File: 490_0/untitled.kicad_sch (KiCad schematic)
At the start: 37 parts, among them J2 BM04B-PASS-1-TFT, J3 BM04B-PASS-1-TFT, U2 TPS2553DBVR, U3 TPS2553DBVR, U4 USB2512B-I/M2, Y1 24 MHz

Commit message: Final Fixes
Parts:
- renumbered C16 to C10, C17 to C11, C18 to C12, C19 to C13, C20 to C14, C21 to C15, C22 to C16, C23 to C17, C24 to C18, C9 to C3, C10 to C4, C11 to C5, C12 to C6, C13 to C7, C14 to C8, C15 to C9, R22 to R10, R23 to R11, R15 to R3, R16 to R4, R17 to R5, R18 to R6, R19 to R7, R20 to R8, R21 to R9

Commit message: USB hub fix
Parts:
- added C53, C54: 0.1u, symbol PCM_Elektuur:C
- added R45: 10k, symbol Device:R
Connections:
- net +3.3V: now also R45.1
- net GND: now also C53.1 (+), C54.1 (+)
- net HUB_RESET_N: now also R45.2
- net at U4.14 (CRFILT): now also C54.2 (-)
- net at U4.34 (PLLFILT): now also C53.2 (-)
- no-connect marks 13 -> 11
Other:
- moved on the sheet: C17, C18, D3, D4, J2, J3, R10, R11, R7, R8, R9, U4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

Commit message: small update
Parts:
- J2, J3: now not fitted
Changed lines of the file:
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@@
 		(in_bom yes)
 		(on_board yes)
-		(dnp no)
+		(dnp yes)
 		(fields_autoplaced yes)
 		(property "Reference" "J3"
@@
 		(in_bom yes)
 		(on_board yes)
-		(dnp no)
+		(dnp yes)
 		(fields_autoplaced yes)
 		(property "Reference" "J2"

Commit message: Implemented Dmitry recommendations
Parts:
- removed R10, R11, R8, R9: 36k, symbol Device:R
- J2, J3: now fitted; now left out of the parts list
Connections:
- net GND: now also U4.22 (SDA/SMBDATA/NON_REM1), U4.24 (SCL/SMBCLK/CFG_SEL0), U4.25 (HS_IND/CFG_SEL1), U4.28 (SUSP_IN/LOCAL_PWR/NON_REM0)

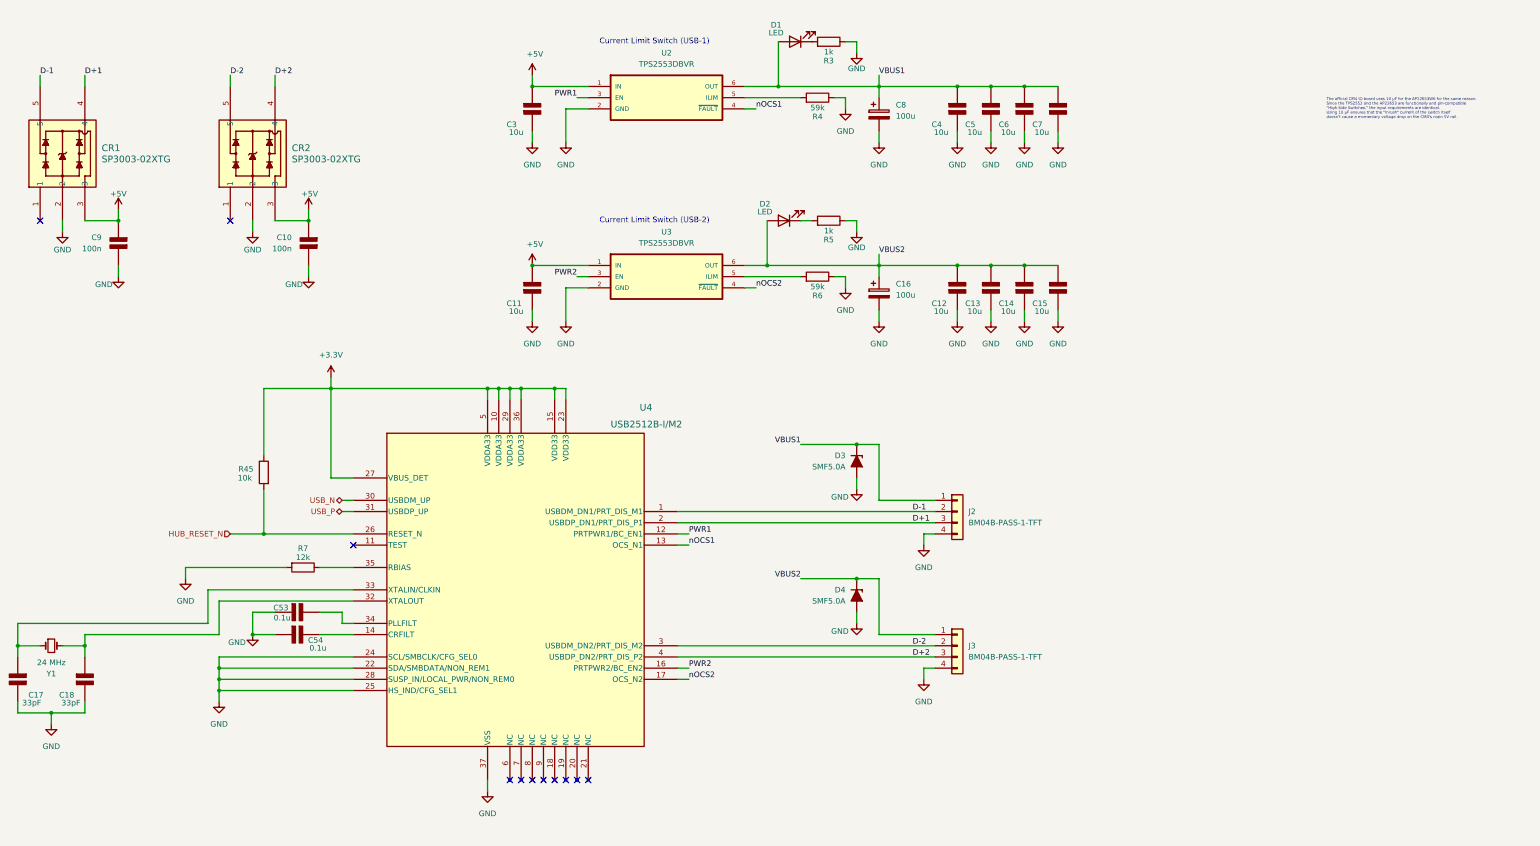
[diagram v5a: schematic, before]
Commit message: Implemented suggestions
notes on schematics:
Overall: Schematics needs to be improved, more compact and cleaner
=========================
I) on root page (page 1):
overall: needs a bit of clean up of the diagram

1. the diagram shows pcb3 and pcb1, but no pcb2, it is probably outdated and therefore might have errors in it, fix it to the latest version and rename things to reflect what it actually is. Also try to clean it up a bit
2. The PCB-3 seem to have the cameras directly connected to the usb hub, how will this be connected? with connectors? if so add them to the diagram, if it's with wires soldered directly to the pcb, try to make note of it for clarity
4. for some reason your TOF is above PCB-3 but is only connected to PCB1, will the TOF be on the glasses, or will you be moving this to the main board? maybe have TOF on the chest for depth, and 2 cameras on glasses for vision, it will also reduce length of cable, which is ideal, i don't think it will work if you run it from the glasses to pcb1 though.
I know, this is a problem, we discussed the chest thing, the problem is the length of the cable but also the haptic feedback is weird if they turn their head.
5. Rename PCB1/PCB3 to PCB1 (chest) PCB3 (glasses) for clarity. Also i don't think (mayeb i'm wrong) that the 5 conected buttons should be on a bus, a bus implies that multiple devices communicate on the same single line. You're using individual lines for each to individual gpio, no?

=========================
II) on PCB-3 usb 2.0 bridge page (page 10)
overall: check datasheet and make sure you've done the connection right and values are selected properly, with the chip data lines properly pulled up/down whether externally or internally. This is important

1. C3/C11 are the input capacitors to U2/u3 TPS553DBVR, datasheet says 100nF, you used 10uF, why? stick to 100nF
2. you seem to have implemented one of /Uthe typical application circuit, look at the others. You have on page 21 of datasheet an auto-retry wi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
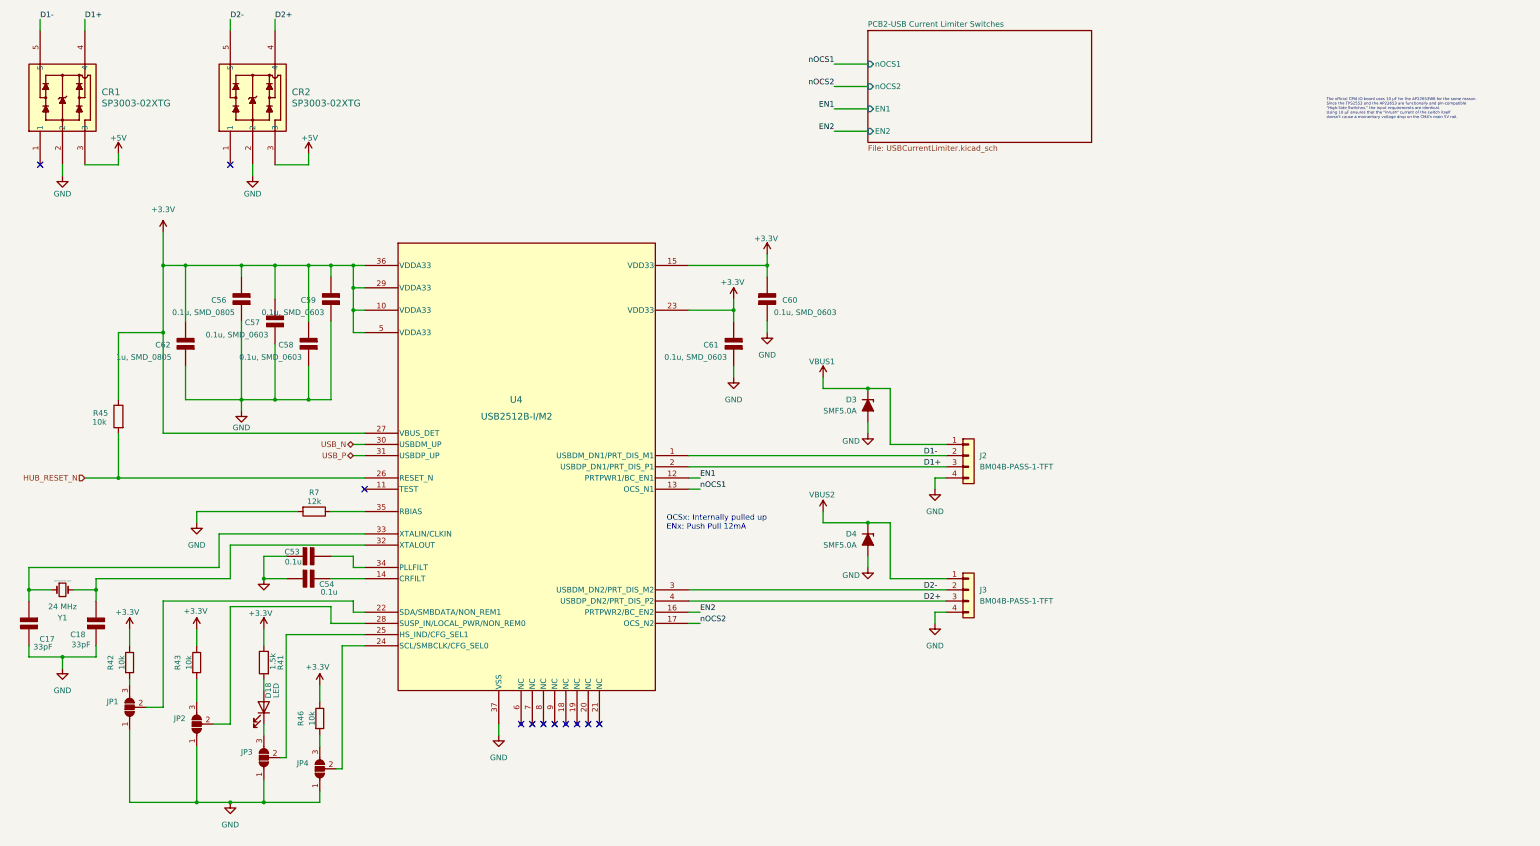
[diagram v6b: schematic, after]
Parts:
- removed C10, C9: 100n, symbol PCM_Elektuur:C
- removed C11, C12, C13, C14, C15, C3, C4, C5, C6, C7: 10u, symbol PCM_Elektuur:C
- removed C16, C8: 100u, symbol Device:C_Polarized
- removed D1, D2: LED, symbol Device:LED
- removed R3, R5: 1k, symbol Device:R
- removed R4, R6: 59k, symbol Device:R
- removed U2, U3: TPS2553DBVR, TPS2553DBVR:SOT95P280X145-6N, symbol capstone_parts:TPS2553DBVR
- added C56: 0.1u, SMD_0805, symbol PCM_Elektuur:C
- added C57, C58, C59, C60, C61: 0.1u, SMD_0603, symbol PCM_Elektuur:C
- added C62: 1u, SMD_0805, symbol PCM_Elektuur:C
- added D18: LED, symbol Device:LED
- added JP1, JP2, JP3, JP4: ~, symbol Jumper:SolderJumper_3_Open
- added R41: 1.5k, symbol Device:R
- added R42, R43, R46: 10k, Resistor_THT:R_Axial_DIN0207_L6.3mm_D2.5mm_P10.16mm_Horizontal, symbol PCM_SL_Resistors:Resistor
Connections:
- net +3.3V: now also C56.2 (-), C57.2 (-), C58.2 (-), C59.2 (-), C60.2 (-), C61.2 (-), C62.2 (-), R41.1, R42.2, R43.2, R46.2
- net GND: now also C56.1 (+), C57.1 (+), C58.1 (+), C59.1 (+), C60.1 (+), C61.1 (+), C62.1 (+), JP1.1 (A), JP2.1 (A), JP3.1 (A), JP4.1 (A); no longer U4.22 (SDA/SMBDATA/NON_REM1), U4.24 (SCL/SMBCLK/CFG_SEL0), U4.25 (HS_IND/CFG_SEL1), U4.28 (SUSP_IN/LOCAL_PWR/NON_REM0)
- net D+1 renamed D1+
- net D+2 renamed D2+
- net D-1 renamed D1-
- net D-2 renamed D2-
- net PWR1 renamed EN1
- net PWR2 renamed EN2
- new net: JP1.2 (C), U4.22 (SDA/SMBDATA/NON_REM1)
- new net: JP1.3 (B), R42.1
- new net: JP2.2 (C), U4.28 (SUSP_IN/LOCAL_PWR/NON_REM0)
- new net: JP2.3 (B), R43.1
- new net: JP4.2 (C), U4.24 (SCL/SMBCLK/CFG_SEL0)
- new net: JP4.3 (B), R46.1
- new net: D18.2 (A), R41.2
- new net: JP3.2 (C), U4.25 (HS_IND/CFG_SEL1)
- new net: D18.1 (K), JP3.3 (B)
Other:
- added sheet PCB2-USB Current Limiter Switches (USBCurrentLimiter.kicad_sch)
- note added: "OCSx: Internally pulled up ENx: Push Pull 12mA"
- note removed: "Current Limit Switch (USB-1)"
- note removed: "Current Limit Switch (USB-2)"
- moved on the sheet: C17, C18, C53, C54, CR1, CR2, D3, D4, J2, J3, R45, R7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

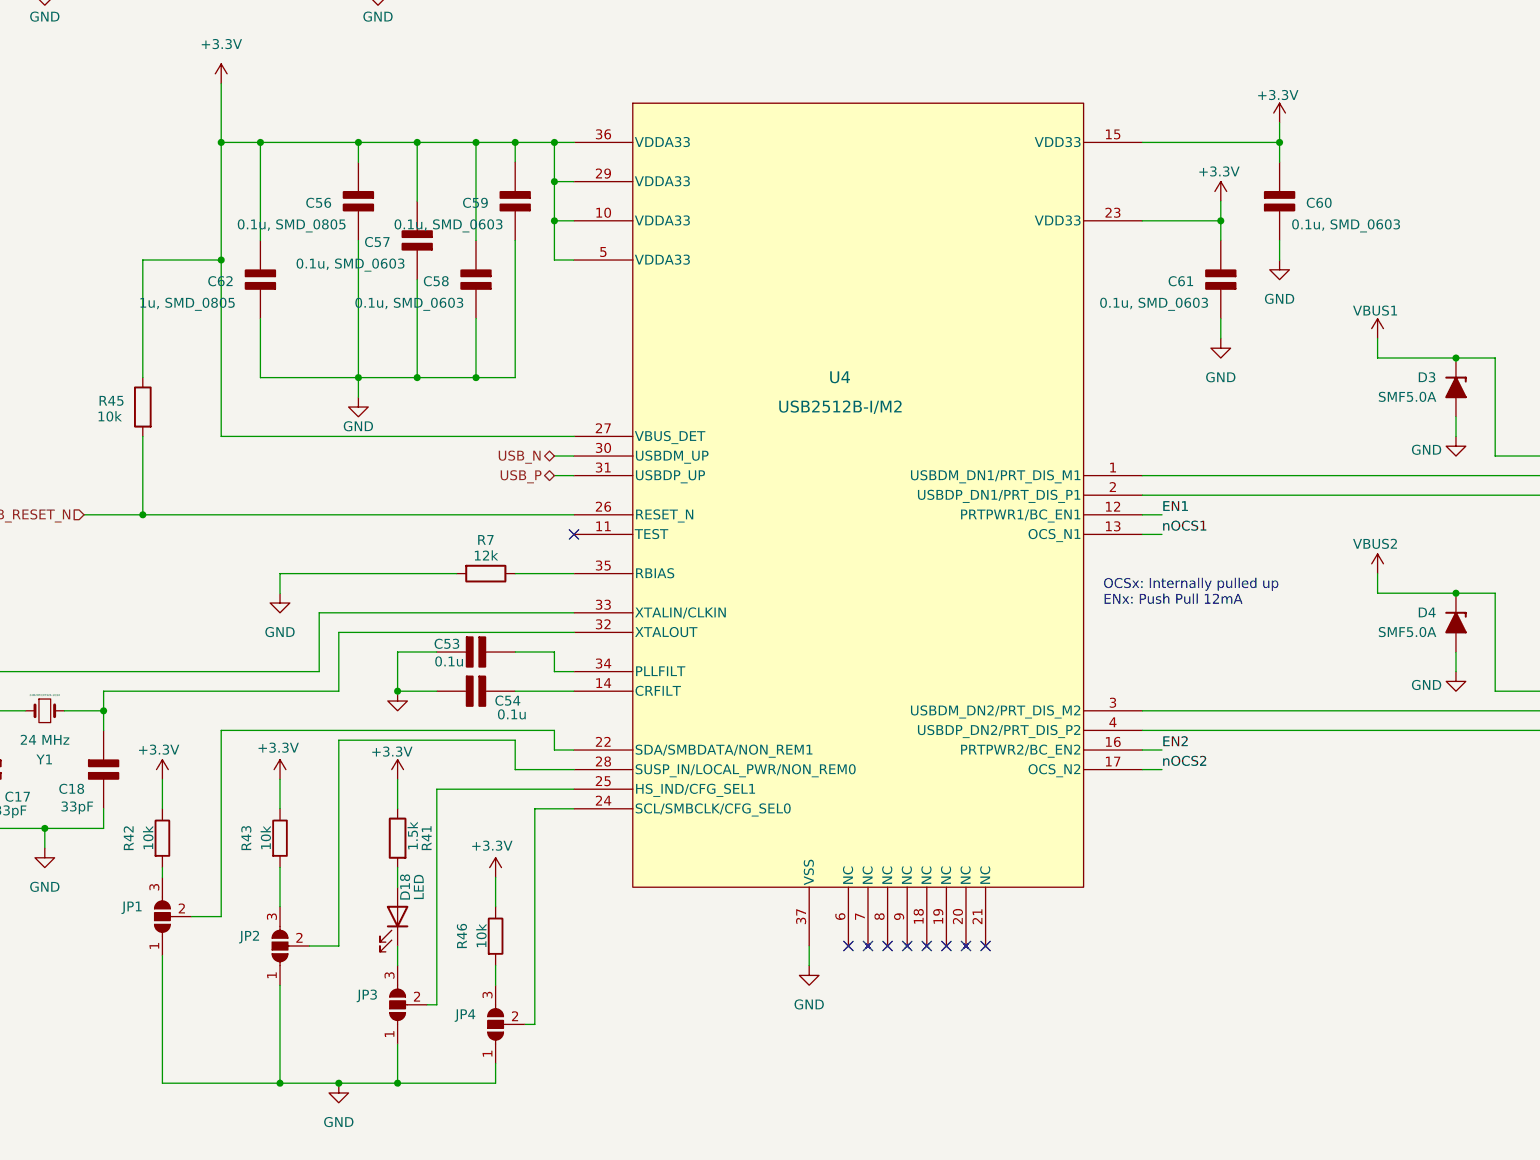
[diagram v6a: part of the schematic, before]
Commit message: FFC to HDMI change
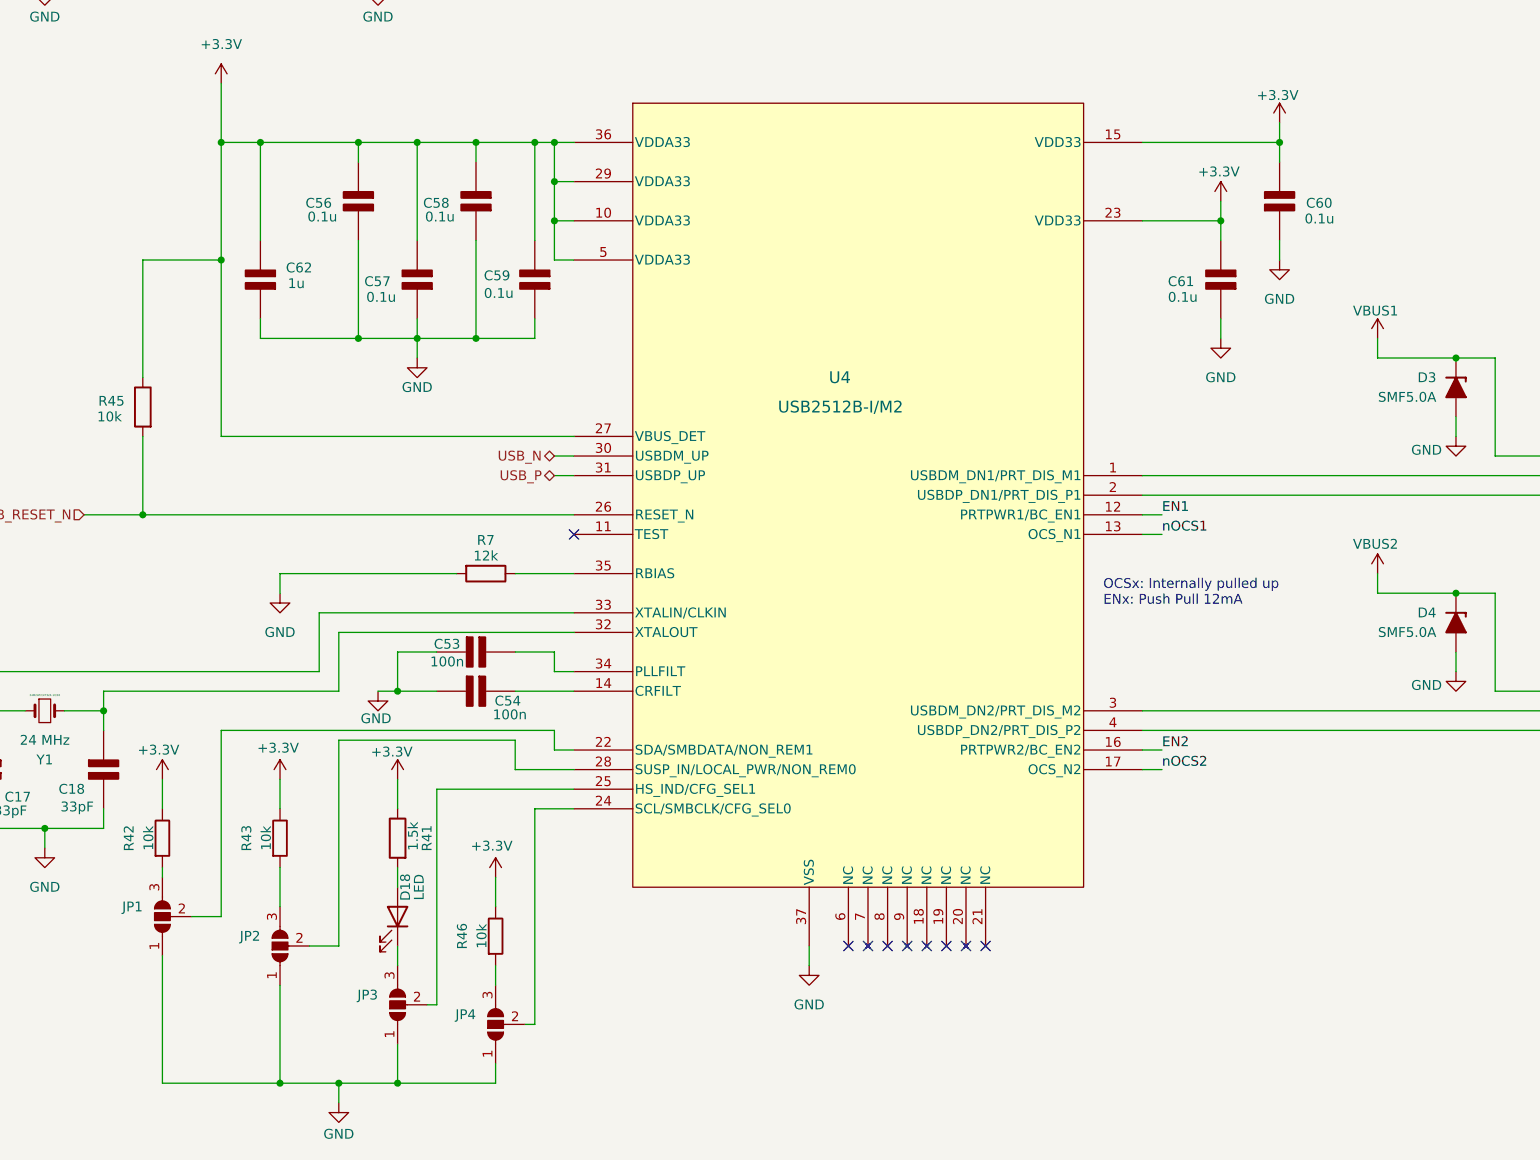
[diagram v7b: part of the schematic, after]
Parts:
- C53, C54: value 0.1u -> 100n
- C56: value 0.1u, SMD_0805 -> 0.1u; Digikey Link (none) -> https://www.digikey.ca/en/products/detail/yageo/CC0805JRX7R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; Manufacturer (none) -> YAGEO; Manufacturer Part (none) -> CC0805JRX7R7BB104; Package (none) -> 0805; Price (none) -> 0.11; Supplier (none) -> DigiKey; Supplier P/N (none) -> 311-4266-1-ND; Type (none) -> SMD, MLCC; Unit (none) -> pcs
- C57, C58, C59, C60, C61: value 0.1u, SMD_0603 -> 0.1u; Digikey Link (none) -> https://www.digikey.ca/en/products/detail/yageo/CC0805JRX7R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; Manufacturer (none) -> YAGEO; Manufacturer Part (none) -> CC0805JRX7R7BB104; Package (none) -> 0805; Price (none) -> 0.11; Supplier (none) -> DigiKey; Supplier P/N (none) -> 311-4266-1-ND; Type (none) -> SMD, MLCC; Unit (none) -> pcs
- C62: value 1u, SMD_0805 -> 1u; Digikey Link (none) -> https://www.digikey.ca/en/products/detail/yageo/CC0805JKX7R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; Manufacturer (none) -> YAGEO; Manufacturer Part (none) -> CC0805JKX7R8BB105; Package (none) -> 0805; Price (none) -> 0.13; Supplier (none) -> DigiKey; Supplier P/N (none) -> 13-CC0805JKX7R8BB105CT-ND; Type (none) -> SMD, MLCC; Unit (none) -> pcs
- R42, R43, R46: Digikey Link (none) -> https://www.digikey.ca/en/products/detail/yageo/RC1206FR-07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; Manufacturer (none) -> YAGEO; Manufacturer Part (none) -> RC1206FR-0710KL; Package (none) -> 1206; Price (none) -> 0.1; Supplier (none) -> DigiKey; Supplier P/N (none) -> 311-10.0KFRCT-ND; Type (none) -> SMD; Unit (none) -> pcs
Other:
- moved on the sheet: C57, C58, C59
